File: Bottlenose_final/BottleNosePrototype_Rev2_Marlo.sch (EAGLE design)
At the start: 29 parts, among them Q1 8/16/20MHz, U1 MCP73831, U2 FT232RLSSOP, X1 USB-SMD-NS

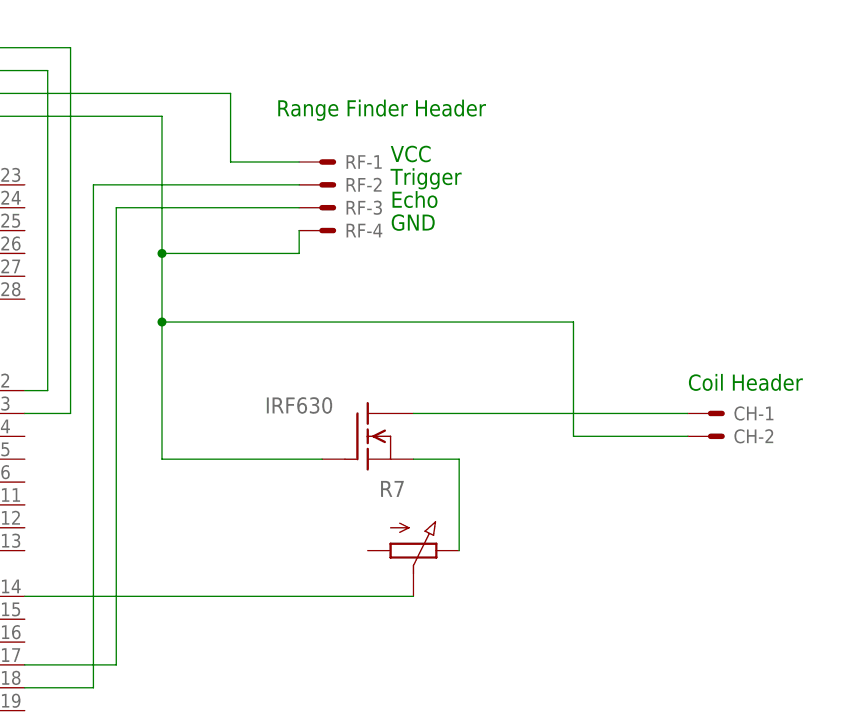
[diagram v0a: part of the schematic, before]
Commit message: added flyback diode and changed MOSFET wiring.
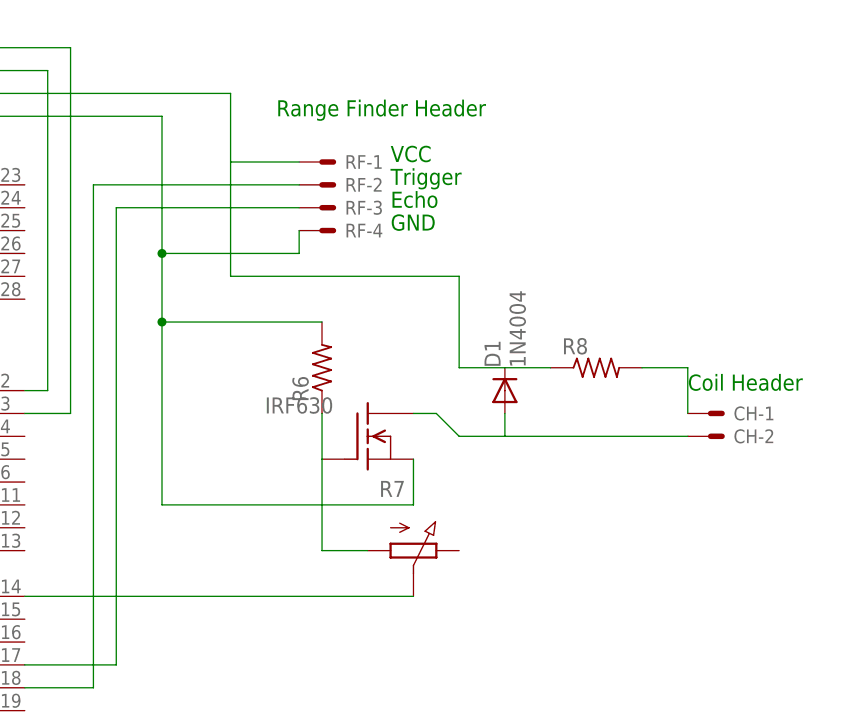
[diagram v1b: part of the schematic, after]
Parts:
- added D1: 1N4004, diode:1N4004
- added R6, R8: (no value), rcl:R-US_0204/5
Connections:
- new net N$46: CH-2.S, D1.A, IRF630.D
- net GND: now also IRF630.S, R6.2; no longer CH-2.S, IRF630.G
- net N$1: now also IRF630.G, R6.1, R7.A; no longer IRF630.S, R7.E
- net N$11: now also R8.2; no longer IRF630.D
- net N$35: now also D1.C, R8.1
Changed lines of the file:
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@@
-<?xml version="1.0" encoding="utf-8"?>
 <!DOCTYPE eagle SYSTEM "eagle.dtd">
 <eagle version="6.4">
@@
 <part name="R7" library="pot-vitrohm" deviceset="PC25" device=""/>
 <part name="IC1" library="v-reg" deviceset="78LXX" device=""/>
+<part name="D1" library="diode" deviceset="1N4004" device=""/>
+<part name="R6" library="rcl" deviceset="R-US_" device="0204/5"/>
+<part name="R8" library="rcl" deviceset="R-US_" device="0204/5"/>
 </parts>
 <sheets>
@@
 <instance part="R7" gate="G" x="144.78" y="30.48" rot="R270"/>
 <instance part="IC1" gate="1" x="17.78" y="35.56"/>
+<instance part="D1" gate="1" x="154.94" y="48.26" rot="R90"/>
+<instance part="R6" gate="G$1" x="134.62" y="50.8" rot="R90"/>
+<instance part="R8" gate="G$1" x="165.1" y="50.8"/>
 </instances>
 <busses>
@@
 <wire x1="116.84" y1="63.5" x2="132.08" y2="63.5" width="0.1524" layer="91"/>
 <wire x1="132.08" y1="63.5" x2="132.08" y2="66.04" width="0.1524" layer="91"/>
-<pinref part="IRF630" gate="G$1" pin="G"/>
-<wire x1="134.62" y1="40.64" x2="116.84" y2="40.64" width="0.1524" layer="91"/>
-<wire x1="116.84" y1="40.64" x2="116.84" y2="55.88" width="0.1524" layer="91"/>
+<wire x1="116.84" y1="35.56" x2="116.84" y2="55.88" width="0.1524" layer="91"/>
 <junction x="116.84" y="63.5"/>
-<pinref part="CH" gate="-2" pin="S"/>
 <wire x1="116.84" y1="55.88" x2="116.84" y2="63.5" width="0.1524" layer="91"/>
-<wire x1="175.26" y1="43.18" x2="162.56" y2="43.18" width="0.1524" layer="91"/>
-<wire x1="162.56" y1="43.18" x2="162.56" y2="55.88" width="0.1524" layer="91"/>
-<wire x1="162.56" y1="55.88" x2="116.84" y2="55.88" width="0.1524" layer="91"/>
 <junction x="116.84" y="55.88"/>
+<wire x1="134.62" y1="55.88" x2="116.84" y2="55.88" width="0.1524" layer="91"/>
 <wire x1="43.18" y1="40.64" x2="43.18" y2="27.94" width="0.1524" layer="91"/>
 <wire x1="43.18" y1="27.94" x2="43.18" y2="7.62" width="0.1524" layer="91"/>
@@
 <junction x="-10.16" y="40.64"/>
 <junction x="43.18" y="27.94"/>
+<pinref part="R6" gate="G$1" pin="2"/>
+<pinref part="IRF630" gate="G$1" pin="S"/>
+<wire x1="144.78" y1="40.64" x2="144.78" y2="35.56" width="0.1524" layer="91"/>
+<wire x1="144.78" y1="35.56" x2="116.84" y2="35.56" width="0.1524" layer="91"/>
 </segment>
 <segment>
@@
 <wire x1="101.6" y1="25.4" x2="144.78" y2="25.4" width="0.1524" layer="91"/>
 <pinref part="R7" gate="G" pin="S"/>
-</segment>
-</net>
-<net name="N$11" class="0">
-<segment>
-<pinref part="IRF630" gate="G$1" pin="D"/>
-<pinref part="CH" gate="-1" pin="S"/>
-<wire x1="144.78" y1="45.72" x2="175.26" y2="45.72" width="0.1524" layer="91"/>
 </segment>
 </net>
@@
 </segment>
 </net>
-<net name="N$1" class="0">
-<segment>
-<pinref part="R7" gate="G" pin="E"/>
-<pinref part="IRF630" gate="G$1" pin="S"/>
-<wire x1="149.86" y1="30.48" x2="149.86" y2="40.64" width="0.1524" layer="91"/>
-<wire x1="149.86" y1="40.64" x2="144.78" y2="40.64" width="0.1524" layer="91"/>
-</segment>
-</net>
 <net name="N$35" class="0">
 <segment>
@@
 <pinref part="IC1" gate="1" pin="OUT"/>
 <junction x="25.4" y="35.56"/>
+<wire x1="124.46" y1="73.66" x2="124.46" y2="60.96" width="0.1524" layer="91"/>
+<wire x1="124.46" y1="60.96" x2="149.86" y2="60.96" width="0.1524" layer="91"/>
+<pinref part="D1" gate="1" pin="C"/>
+<wire x1="154.94" y1="50.8" x2="149.86" y2="50.8" width="0.1524" layer="91"/>
+<wire x1="149.86" y1="60.96" x2="149.86" y2="50.8" width="0.1524" layer="91"/>
+<pinref part="R8" gate="G$1" pin="1"/>
+<wire x1="160.02" y1="50.8" x2="154.94" y2="50.8" width="0.1524" layer="91"/>
 </segment>
 </net>
@@
 </segment>
 </net>
+<net name="N$1" class="0">
+<segment>
+<pinref part="R7" gate="G" pin="A"/>
+<pinref part="IRF630" gate="G$1" pin="G"/>
+<wire x1="139.7" y1="30.48" x2="134.62" y2="30.48" width="0.1524" layer="91"/>
+<wire x1="134.62" y1="30.48" x2="134.62" y2="40.64" width="0.1524" layer="91"/>
+<pinref part="R6" gate="G$1" pin="1"/>
+<wire x1="134.62" y1="40.64" x2="134.62" y2="45.72" width="0.1524" layer="91"/>
+</segment>
+</net>
+<net name="N$46" class="0">
+<segment>
+<pinref part="CH" gate="-2" pin="S"/>
+<wire x1="175.26" y1="43.18" x2="154.94" y2="43.18" width="0.1524" layer="91"/>
+<pinref part="D1" gate="1" pin="A"/>
+<wire x1="154.94" y1="43.18" x2="154.94" y2="45.72" width="0.1524" layer="91"/>
+<wire x1="154.94" y1="43.18" x2="149.86" y2="43.18" width="0.1524" layer="91"/>
+<pinref part="IRF630" gate="G$1" pin="D"/>
+<wire x1="149.86" y1="43.18" x2="147.32" y2="45.72" width="0.1524" layer="91"/>
+<wire x1="147.32" y1="45.72" x2="144.78" y2="45.72" width="0.1524" layer="91"/>
+</segment>
+</net>
+<net name="N$11" class="0">
+<segment>
+<pinref part="CH" gate="-1" pin="S"/>
+<wire x1="175.26" y1="50.8" x2="175.26" y2="45.72" width="0.1524" layer="91"/>
+<pinref part="R8" gate="G$1" pin="2"/>
+<wire x1="170.18" y1="50.8" x2="175.26" y2="50.8" width="0.1524" layer="91"/>
+</segment>
+</net>

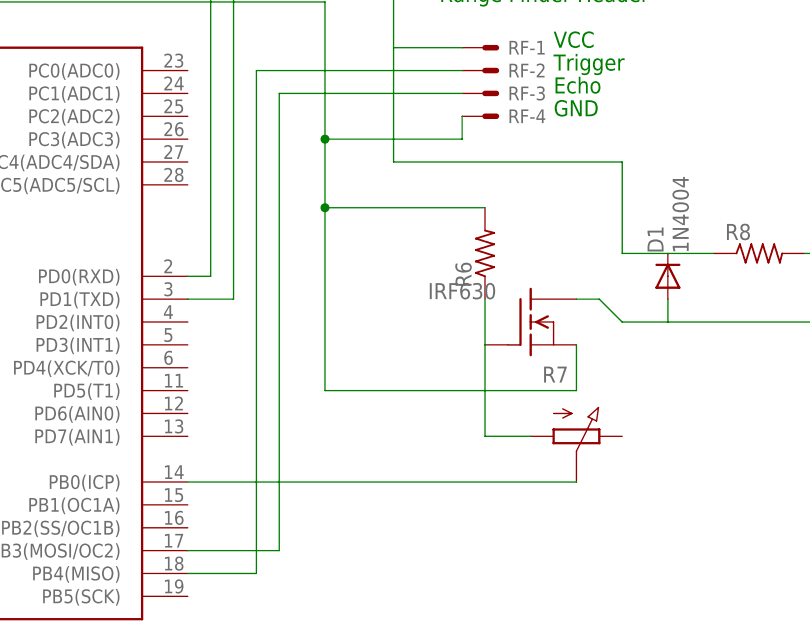
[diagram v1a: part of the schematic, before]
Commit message: added flyback diode and changed mosfet wiring. also, moved trim pot to coil line, mikers idea.
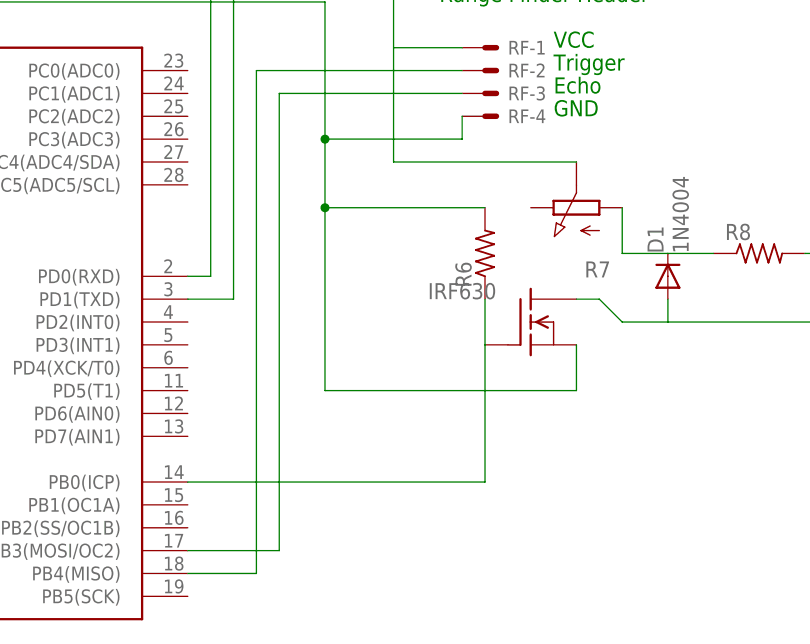
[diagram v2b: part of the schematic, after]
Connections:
- net N$1: now also ATMEGA328.PB0(ICP); no longer R7.A
- net N$10: now also D1.C, R7.A, R8.1; no longer ATMEGA328.PB0(ICP), R7.S
- net N$35: now also R7.S; no longer D1.C, R8.1
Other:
- moved on the sheet: R7
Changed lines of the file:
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@@
 </instance>
 <instance part="GND15" gate="1" x="35.56" y="43.18"/>
-<instance part="R7" gate="G" x="144.78" y="30.48" rot="R270"/>
+<instance part="R7" gate="G" x="144.78" y="55.88" rot="R90"/>
 <instance part="IC1" gate="1" x="17.78" y="35.56"/>
 <instance part="D1" gate="1" x="154.94" y="48.26" rot="R90"/>
@@
 <pinref part="RF" gate="-2" pin="S"/>
 <wire x1="109.22" y1="71.12" x2="132.08" y2="71.12" width="0.1524" layer="91"/>
-</segment>
-</net>
-<net name="N$10" class="0">
-<segment>
-<pinref part="ATMEGA328" gate="G$1" pin="PB0(ICP)"/>
-<wire x1="101.6" y1="25.4" x2="144.78" y2="25.4" width="0.1524" layer="91"/>
-<pinref part="R7" gate="G" pin="S"/>
 </segment>
 </net>
@@
 <junction x="25.4" y="35.56"/>
 <wire x1="124.46" y1="73.66" x2="124.46" y2="60.96" width="0.1524" layer="91"/>
-<wire x1="124.46" y1="60.96" x2="149.86" y2="60.96" width="0.1524" layer="91"/>
-<pinref part="D1" gate="1" pin="C"/>
-<wire x1="154.94" y1="50.8" x2="149.86" y2="50.8" width="0.1524" layer="91"/>
-<wire x1="149.86" y1="60.96" x2="149.86" y2="50.8" width="0.1524" layer="91"/>
-<pinref part="R8" gate="G$1" pin="1"/>
-<wire x1="160.02" y1="50.8" x2="154.94" y2="50.8" width="0.1524" layer="91"/>
+<wire x1="124.46" y1="60.96" x2="144.78" y2="60.96" width="0.1524" layer="91"/>
+<pinref part="R7" gate="G" pin="S"/>
 </segment>
 </net>
@@
 <net name="N$1" class="0">
 <segment>
-<pinref part="R7" gate="G" pin="A"/>
 <pinref part="IRF630" gate="G$1" pin="G"/>
-<wire x1="139.7" y1="30.48" x2="134.62" y2="30.48" width="0.1524" layer="91"/>
-<wire x1="134.62" y1="30.48" x2="134.62" y2="40.64" width="0.1524" layer="91"/>
+<wire x1="134.62" y1="25.4" x2="134.62" y2="40.64" width="0.1524" layer="91"/>
 <pinref part="R6" gate="G$1" pin="1"/>
 <wire x1="134.62" y1="40.64" x2="134.62" y2="45.72" width="0.1524" layer="91"/>
+<pinref part="ATMEGA328" gate="G$1" pin="PB0(ICP)"/>
+<wire x1="101.6" y1="25.4" x2="134.62" y2="25.4" width="0.1524" layer="91"/>
 </segment>
 </net>
@@
 </segment>
 </net>
+<net name="N$10" class="0">
+<segment>
+<pinref part="D1" gate="1" pin="C"/>
+<pinref part="R8" gate="G$1" pin="1"/>
+<wire x1="160.02" y1="50.8" x2="154.94" y2="50.8" width="0.1524" layer="91"/>
+<wire x1="154.94" y1="50.8" x2="149.86" y2="50.8" width="0.1524" layer="91"/>
+<pinref part="R7" gate="G" pin="A"/>
+<wire x1="149.86" y1="55.88" x2="149.86" y2="50.8" width="0.1524" layer="91"/>
+</segment>
+</net>

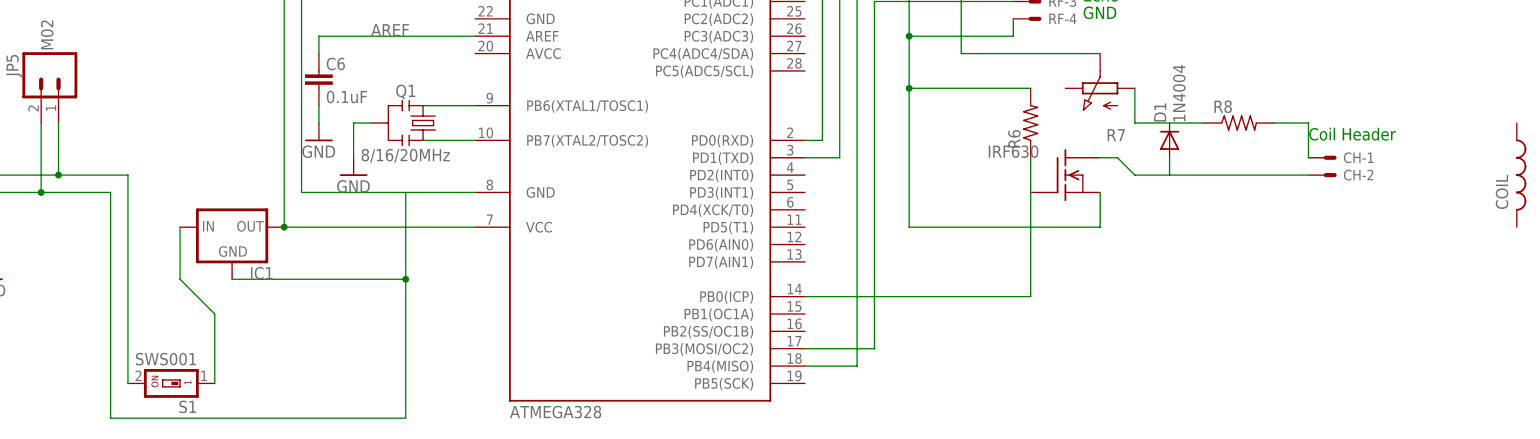
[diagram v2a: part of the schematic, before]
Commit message: Removed switch from the .sch and replaced it with a switch header.
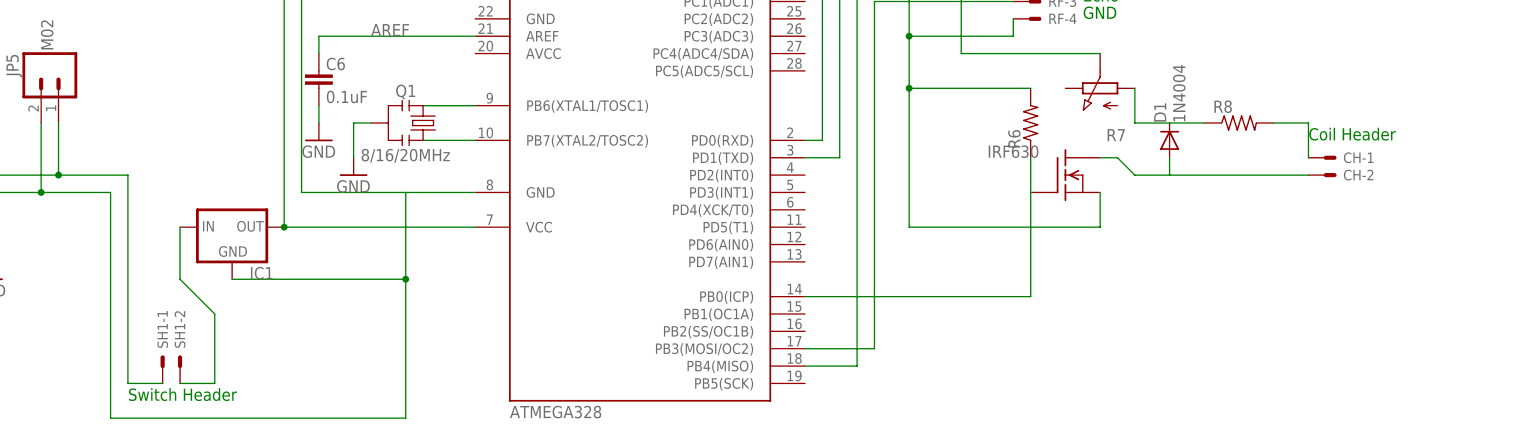
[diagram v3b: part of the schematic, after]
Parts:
- removed COIL: (no value), rcl:L-US0204/7
- removed S1: SWS001, smd-special:SWS001
- added SH1: 22-23-2021, con-molex:22-23-2021
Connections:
- net N$5: now also SH1-2.S; no longer S1.1
- net VBAT: now also SH1-1.S; no longer S1.2
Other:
- note added: "Switch Header"
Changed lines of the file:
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@@
+<?xml version="1.0" encoding="utf-8"?>
 <!DOCTYPE eagle SYSTEM "eagle.dtd">
-<eagle version="6.4">
+<eagle version="6.2">
 <drawing>
 <settings>
@@
 <part name="GND7" library="SparkFun" deviceset="GND" device=""/>
 <part name="LED1" library="SparkFun" deviceset="LED" device="3MM" value="DNP"/>
-<part name="COIL" library="rcl" deviceset="L-US" device="0204/7"/>
 <part name="CH" library="con-molex" deviceset="22-23-2021" device="" value=""/>
-<part name="S1" library="smd-special" deviceset="SWS001" device=""/>
 <part name="C3" library="SparkFun" deviceset="CAP" device="0402-CAP" value="0.1uF"/>
 <part name="C5" library="SparkFun" deviceset="CAP_POL" device="1206" value="10uF"/>
@@
 <part name="R6" library="rcl" deviceset="R-US_" device="0204/5"/>
 <part name="R8" library="rcl" deviceset="R-US_" device="0204/5"/>
+<part name="SH1" library="con-molex" deviceset="22-23-2021" device="" value=""/>
 </parts>
 <sheets>
@@
 <text x="129.54" y="78.74" size="1.778" layer="91">Range Finder Header</text>
 <text x="175.26" y="48.26" size="1.778" layer="91">Coil Header</text>
+<text x="2.54" y="10.16" size="1.778" layer="91">Switch Header</text>
 </plain>
 <instances>
@@
 <instance part="GND7" gate="1" x="-17.78" y="27.94"/>
 <instance part="LED1" gate="G$1" x="-111.76" y="66.04"/>
-<instance part="COIL" gate="G$1" x="205.74" y="43.18"/>
 <instance part="CH" gate="-1" x="177.8" y="45.72"/>
 <instance part="CH" gate="-2" x="177.8" y="43.18"/>
-<instance part="S1" gate="G$1" x="10.16" y="12.7" rot="R90"/>
 <instance part="C3" gate="G$1" x="-27.94" y="119.38"/>
 <instance part="C5" gate="G$1" x="-17.78" y="121.92"/>
@@
 <instance part="R6" gate="G$1" x="134.62" y="50.8" rot="R90"/>
 <instance part="R8" gate="G$1" x="165.1" y="50.8"/>
+<instance part="SH1" gate="-1" x="7.62" y="15.24" rot="R90"/>
+<instance part="SH1" gate="-2" x="10.16" y="15.24" rot="R90"/>
 </instances>
 <busses>
@@
 <pinref part="C2" gate="G$1" pin="1"/>
 <wire x1="2.54" y1="43.18" x2="2.54" y2="12.7" width="0.1524" layer="91"/>
-<pinref part="S1" gate="G$1" pin="2"/>
 <wire x1="2.54" y1="43.18" x2="-7.62" y2="43.18" width="0.1524" layer="91"/>
 <pinref part="JP5" gate="G$1" pin="1"/>
@@
 <wire x1="-7.62" y1="50.8" x2="-7.62" y2="43.18" width="0.1524" layer="91"/>
 <junction x="-7.62" y="43.18"/>
+<pinref part="SH1" gate="-1" pin="S"/>
+<wire x1="2.54" y1="12.7" x2="7.62" y2="12.7" width="0.1524" layer="91"/>
 </segment>
 </net>
@@
 <wire x1="10.16" y1="35.56" x2="10.16" y2="27.94" width="0.1524" layer="91"/>
 <wire x1="10.16" y1="27.94" x2="15.24" y2="22.86" width="0.1524" layer="91"/>
-<pinref part="S1" gate="G$1" pin="1"/>
 <wire x1="15.24" y1="22.86" x2="15.24" y2="12.7" width="0.1524" layer="91"/>
-</segment>
-</net>
+<pinref part="SH1" gate="-2" pin="S"/>
+<wire x1="10.16" y1="12.7" x2="15.24" y2="12.7" width="0.1524" layer="91"/>
+</segment>
+</net>
